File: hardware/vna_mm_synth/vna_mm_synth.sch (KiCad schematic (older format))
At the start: 0 parts

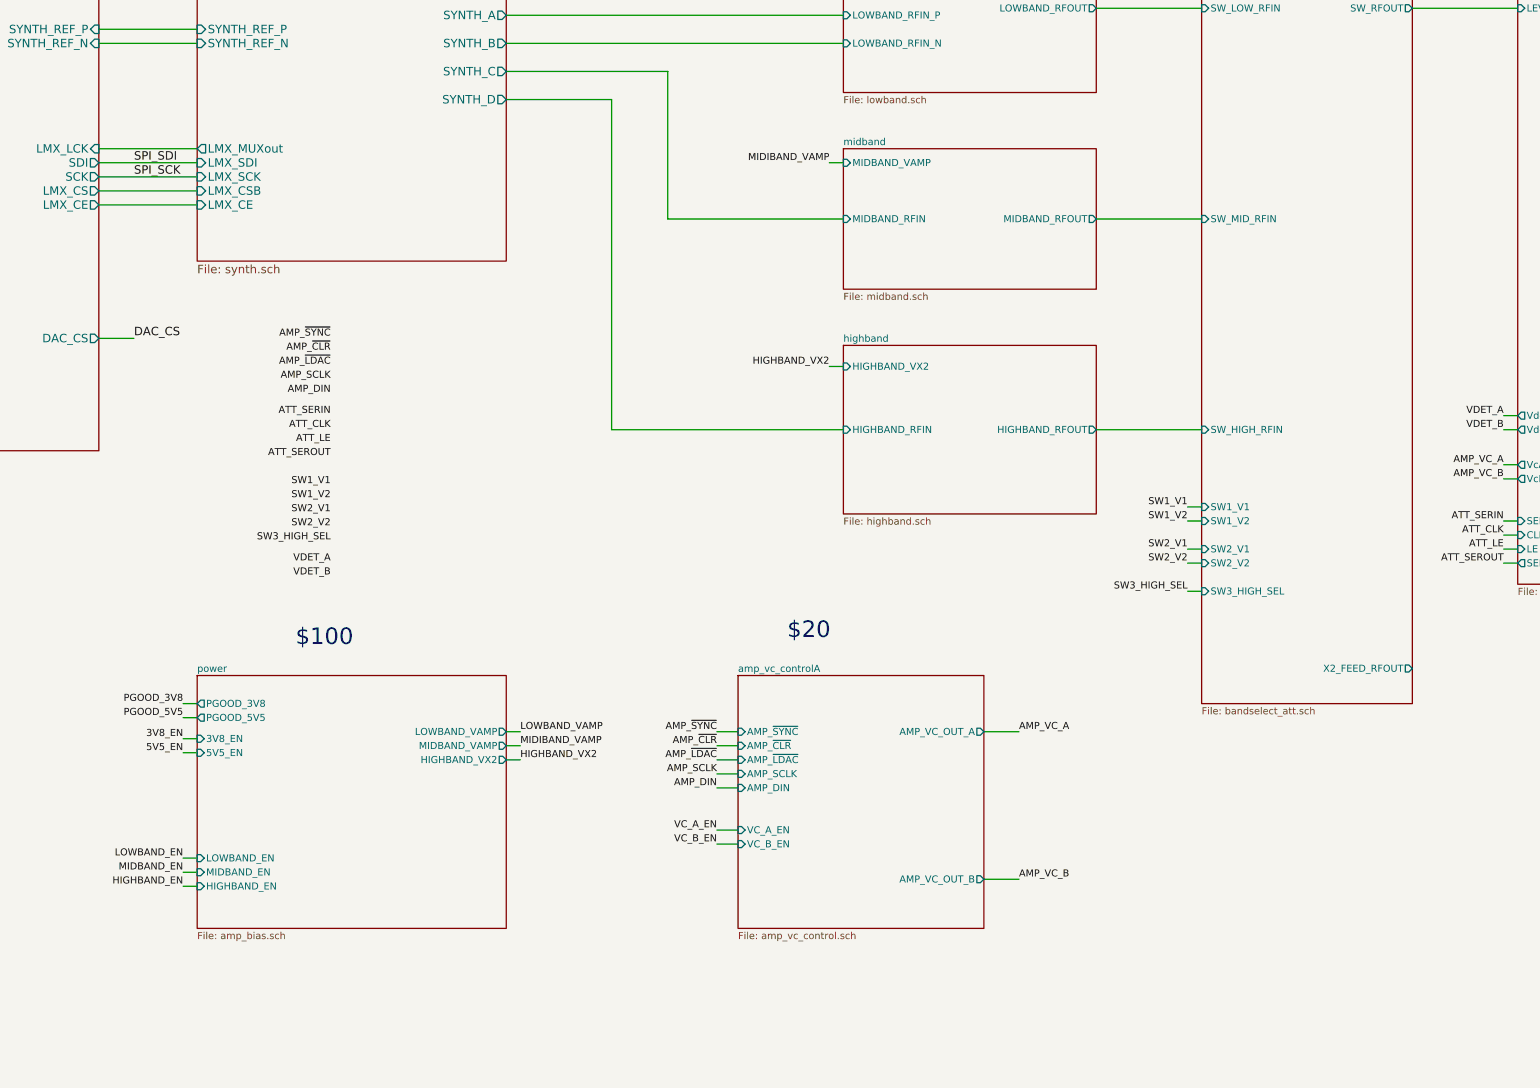
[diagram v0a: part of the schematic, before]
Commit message: changed synth midband filter bank to admv8416, added rf test points
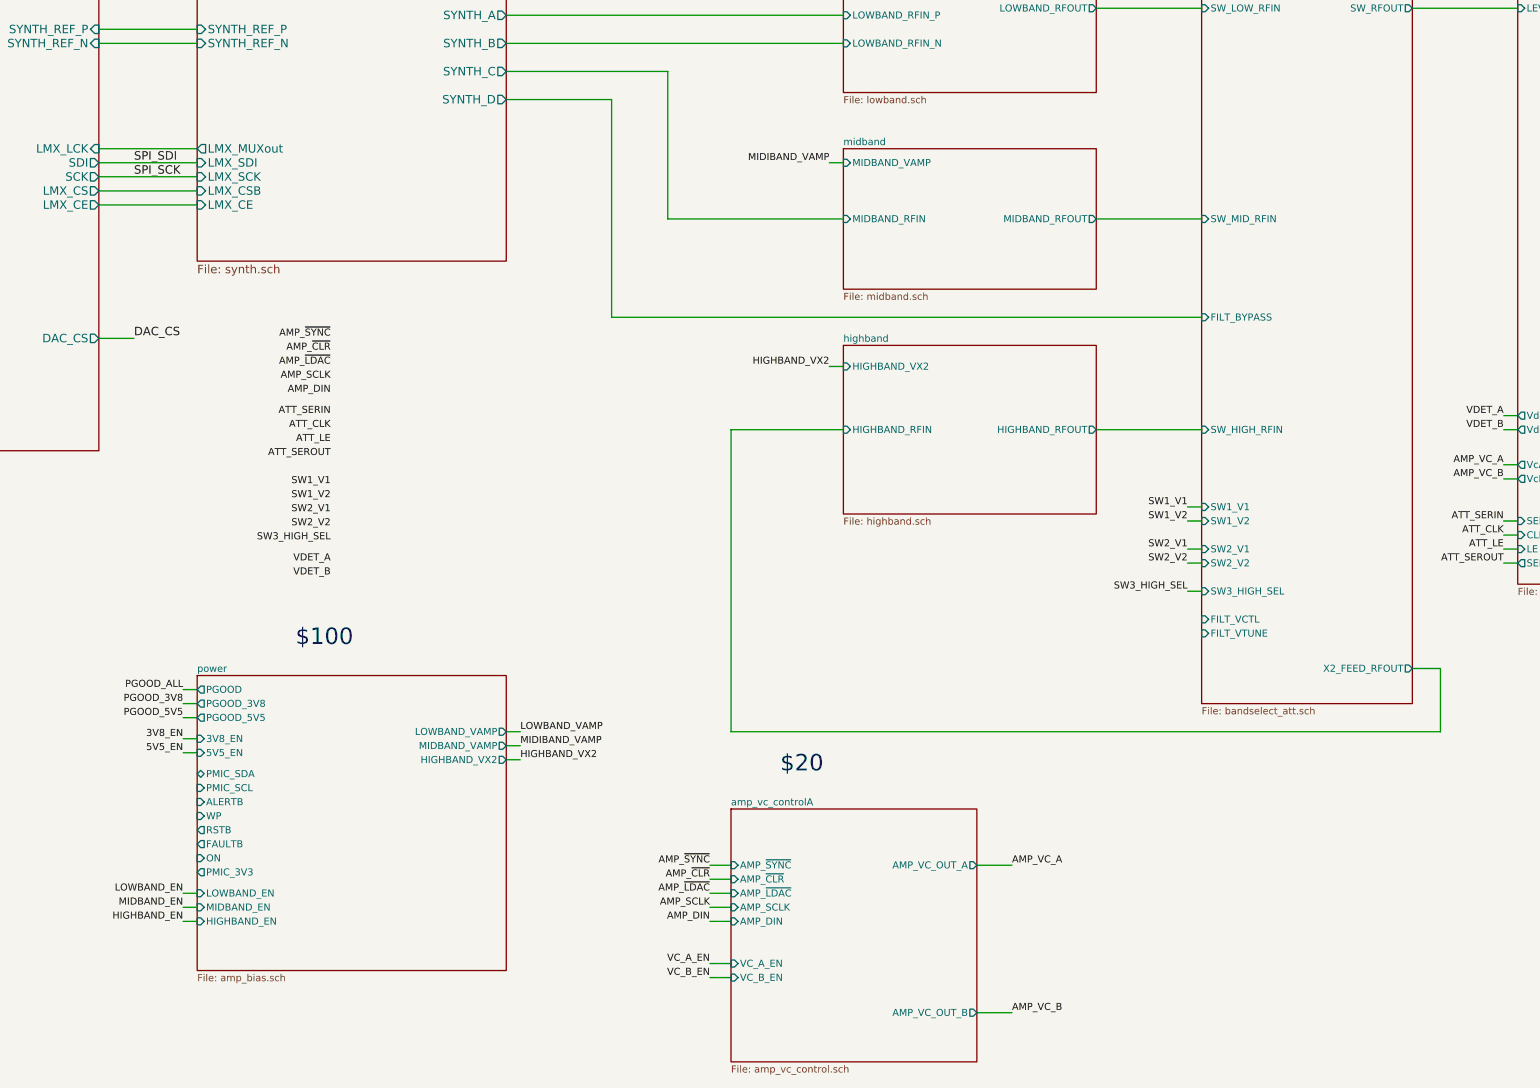
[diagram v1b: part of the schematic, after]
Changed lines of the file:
@@
 goals:\n400 MHz to 26.5 GHz (29 GHz)\n-15 dBc 2nd order harmonics\n-25 dBc 3rd order harmonics\n-15 to 0 dBm output power +/- 1 dB at room\nsettling time >1 ms to 90% amplitude\nphase sync with external reference\nBOM >$1000/each\nenclosure\nice40 fpga controlled?
 Wire Wire Line
-	11550 6050 9900 6050
-Wire Wire Line
-	9900 6050 9900 3700
+	11550 6050 10750 6050
 Wire Wire Line
 	9150 3700 9900 3700
@@
 Text Label 9250 8400 0    50   ~ 0
 HIGHBAND_VX2
-Text Label 12800 8200 0    50   ~ 0
+Text Label 12750 9150 0    50   ~ 0
 AMP_VC_A
-Text Label 12800 9250 0    50   ~ 0
+Text Label 12750 10200 0    50   ~ 0
 AMP_VC_B
 Text Label 11450 2750 2    50   ~ 0
@@
 F10 "SW1_V1" I L 14100 6600 50
 F11 "SW1_V2" I L 14100 6700 50
+F12 "FILT_VCTL" I L 14100 7400 50
+F13 "FILT_VTUNE" I L 14100 7500 50
+F14 "FILT_BYPASS" I L 14100 5250 50
 $EndSheet
 Text Label 14000 7000 2    50   ~ 0
@@
 SW3_HIGH_SEL
 $Sheet
-S 10800 7800 1750 1800
+S 10750 8750 1750 1800
 U 5D8E086E
 F0 "amp_vc_controlA" 50
 F1 "amp_vc_control.sch" 50
-F2 "AMP_VC_OUT_A" O R 12550 8200 50
-F3 "AMP_~SYNC" I L 10800 8200 50
-F4 "AMP_~CLR" I L 10800 8300 50
-F5 "AMP_~LDAC" I L 10800 8400 50
-F6 "AMP_SCLK" I L 10800 8500 50
-F7 "AMP_DIN" I L 10800 8600 50
-F8 "AMP_VC_OUT_B" O R 12550 9250 50
-F9 "VC_B_EN" I L 10800 9000 50
-F10 "VC_A_EN" I L 10800 8900 50
+F2 "AMP_VC_OUT_A" O R 12500 9150 50
+F3 "AMP_~SYNC" I L 10750 9150 50
+F4 "AMP_~CLR" I L 10750 9250 50
+F5 "AMP_~LDAC" I L 10750 9350 50
+F6 "AMP_SCLK" I L 10750 9450 50
+F7 "AMP_DIN" I L 10750 9550 50
+F8 "AMP_VC_OUT_B" O R 12500 10200 50
+F9 "VC_B_EN" I L 10750 9950 50
+F10 "VC_A_EN" I L 10750 9850 50
 $EndSheet
 Wire Wire Line
-	12550 8200 12800 8200
-Wire Wire Line
-	12550 9250 12800 9250
+	12500 9150 12750 9150
+Wire Wire Line
+	12500 10200 12750 10200
 $Sheet
-S 6950 7800 2200 1800
+S 6950 7800 2200 2100
 U 5D4AD94E
 F0 "power" 50
@@
 F7 "3V8_EN" I L 6950 8250 50
 F8 "5V5_EN" I L 6950 8350 50
-F9 "LOWBAND_EN" I L 6950 9100 50
-F10 "MIDBAND_EN" I L 6950 9200 50
-F11 "HIGHBAND_EN" I L 6950 9300 50
+F9 "LOWBAND_EN" I L 6950 9350 50
+F10 "MIDBAND_EN" I L 6950 9450 50
+F11 "HIGHBAND_EN" I L 6950 9550 50
+F12 "PGOOD" O L 6950 7900 50
+F13 "PMIC_SDA" B L 6950 8500 50
+F14 "PMIC_SCL" I L 6950 8600 50
+F15 "ALERTB" I L 6950 8700 50
+F16 "WP" I L 6950 8800 50
+F17 "RSTB" O L 6950 8900 50
+F18 "FAULTB" O L 6950 9000 50
+F19 "ON" I L 6950 9100 50
+F20 "PMIC_3V3" O L 6950 9200 50
 $EndSheet
 Wire Wire Line
-	10800 8200 10650 8200
-Wire Wire Line
-	10800 8300 10650 8300
-Text Label 10650 8200 2    50   ~ 0
+	10750 9150 10600 9150
+Wire Wire Line
+	10750 9250 10600 9250
+Text Label 10600 9150 2    50   ~ 0
 AMP_~SYNC
-Text Label 10650 8300 2    50   ~ 0
+Text Label 10600 9250 2    50   ~ 0
 AMP_~CLR
-Text Label 10650 8400 2    50   ~ 0
+Text Label 10600 9350 2    50   ~ 0
 AMP_~LDAC
-Text Label 10650 8500 2    50   ~ 0
+Text Label 10600 9450 2    50   ~ 0
 AMP_SCLK
-Text Label 10650 8600 2    50   ~ 0
+Text Label 10600 9550 2    50   ~ 0
 AMP_DIN
 Wire Wire Line
-	10650 8400 10800 8400
-Wire Wire Line
-	10650 8500 10800 8500
-Wire Wire Line
-	10650 8600 10800 8600
+	10600 9350 10750 9350
+Wire Wire Line
+	10600 9450 10750 9450
+Wire Wire Line
+	10600 9550 10750 9550
 Wire Wire Line
 	6950 8000 6850 8000
@@
 Wire Wire Line
 	6850 8350 6950 8350
-Text Label 6850 9100 2    50   ~ 0
+Text Label 6850 9350 2    50   ~ 0
 LOWBAND_EN
 Wire Wire Line
-	6850 9100 6950 9100
-Wire Wire Line
-	6850 9200 6950 9200
-Wire Wire Line
-	6850 9300 6950 9300
-Text Label 6850 9200 2    50   ~ 0
+	6850 9350 6950 9350
+Wire Wire Line
+	6850 9450 6950 9450
+Wire Wire Line
+	6850 9550 6950 9550
+Text Label 6850 9450 2    50   ~ 0
 MIDBAND_EN
-Text Label 6850 9300 2    50   ~ 0
+Text Label 6850 9550 2    50   ~ 0
 HIGHBAND_EN
 Text Label 7900 5400 2    50   ~ 0
@@
 Text Notes 7650 7600 0    118  ~ 0
 $100
-Text Notes 11150 7550 0    118  ~ 0
+Text Notes 11100 8500 0    118  ~ 0
 $20
 Text Label 7900 7000 2    50   ~ 0
@@
 Text Label 7900 7100 2    50   ~ 0
 VDET_B
-Text Label 10650 8900 2    50   ~ 0
+Text Label 10600 9850 2    50   ~ 0
 VC_A_EN
-Text Label 10650 9000 2    50   ~ 0
+Text Label 10600 9950 2    50   ~ 0
 VC_B_EN
 Wire Wire Line
-	10650 9000 10800 9000
-Wire Wire Line
-	10800 8900 10650 8900
+	10600 9950 10750 9950
+Wire Wire Line
+	10750 9850 10600 9850
+Text Label 6850 7900 2    50   ~ 0
+PGOOD_ALL
+Wire Wire Line
+	6850 7900 6950 7900
+Wire Wire Line
+	15600 7750 15800 7750
+Wire Wire Line
+	15800 7750 15800 8200
+Wire Wire Line
+	15800 8200 10750 8200
+Wire Wire Line
+	10750 8200 10750 6050
+Wire Wire Line
+	14100 5250 9900 5250
+Wire Wire Line
+	9900 5250 9900 3700
 $EndSCHEMATC

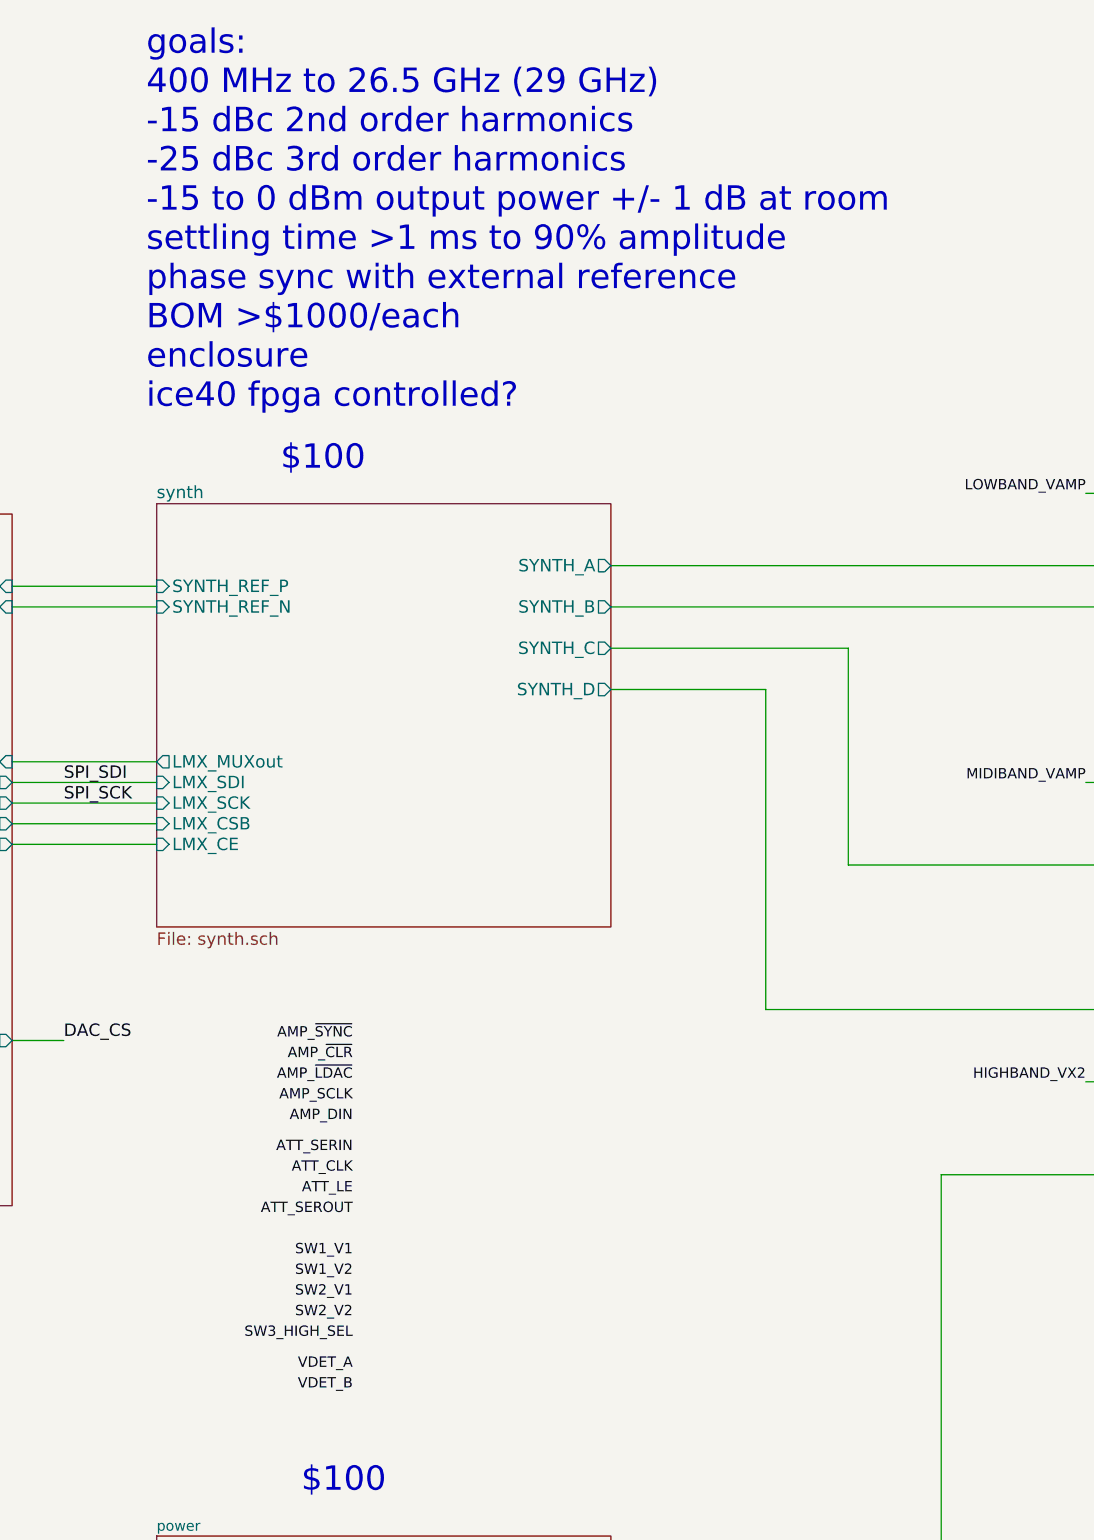
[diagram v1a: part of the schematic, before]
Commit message: added trl cal and set of breakout boards
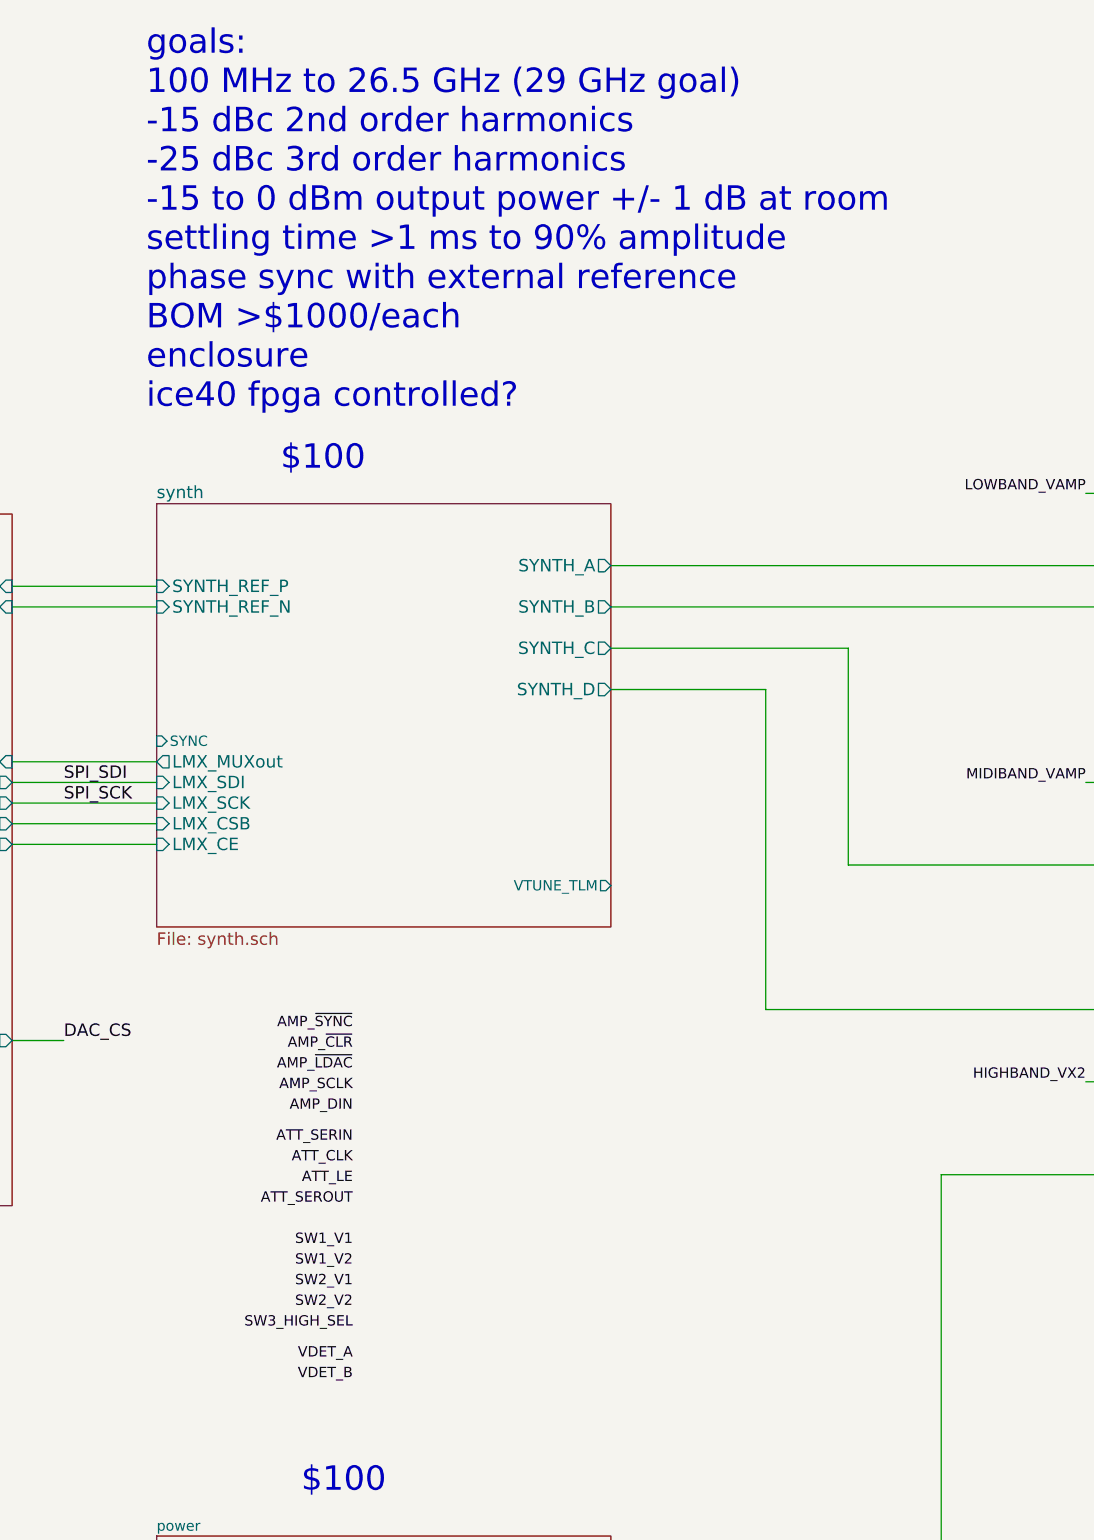
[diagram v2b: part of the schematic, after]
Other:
- note added: "goals:\n100 MHz to 26.5 GHz (29 GHz goal)\n-15 dBc 2nd order harmonics\n-25 dBc 3rd order harmonics\n-15 to 0 dBm output power +/- 1 dB at room\nsettling time >1 ms to 90% amplitude\nphase sync with external reference\nBOM >$1000/each\nenclosure\nice40 fpga controlled?"
- note removed: "goals:\n400 MHz to 26.5 GHz (29 GHz)\n-15 dBc 2nd order harmonics\n-25 dBc 3rd order harmonics\n-15 to 0 dBm output power +/- 1 dB at room\nsettling time >1 ms to 90% amplitude\nphase sync with external reference\nBOM >$1000/each\nenclosure\nice40 fpga controlled?"
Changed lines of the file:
@@
 F11 "LMX_SDI" I L 6950 4150 60
 F12 "LMX_SCK" I L 6950 4250 60
+F13 "SYNC" I L 6950 3950 50
+F14 "VTUNE_TLM" O R 9150 4650 50
 $EndSheet
 $Sheet
@@
 $EndSheet
 Text Notes 6900 2350 0    118  ~ 0
-goals:\n400 MHz to 26.5 GHz (29 GHz)\n-15 dBc 2nd order harmonics\n-25 dBc 3rd order harmonics\n-15 to 0 dBm output power +/- 1 dB at room\nsettling time >1 ms to 90% amplitude\nphase sync with external reference\nBOM >$1000/each\nenclosure\nice40 fpga controlled?
+goals:\n100 MHz to 26.5 GHz (29 GHz goal)\n-15 dBc 2nd order harmonics\n-25 dBc 3rd order harmonics\n-15 to 0 dBm output power +/- 1 dB at room\nsettling time >1 ms to 90% amplitude\nphase sync with external reference\nBOM >$1000/each\nenclosure\nice40 fpga controlled?
 Wire Wire Line
 	11550 6050 10750 6050
@@
 Wire Wire Line
 	16250 7000 16350 7000
-Text Label 7900 5950 2    50   ~ 0
+Text Label 7900 5900 2    50   ~ 0
 ATT_SERIN
-Text Label 7900 6050 2    50   ~ 0
+Text Label 7900 6000 2    50   ~ 0
 ATT_CLK
-Text Label 7900 6150 2    50   ~ 0
+Text Label 7900 6100 2    50   ~ 0
 ATT_LE
-Text Label 7900 6250 2    50   ~ 0
+Text Label 7900 6200 2    50   ~ 0
 ATT_SEROUT
 Wire Wire Line
@@
 Text Label 14000 7200 2    50   ~ 0
 SW3_HIGH_SEL
-Text Label 7900 6450 2    50   ~ 0
+Text Label 7900 6400 2    50   ~ 0
 SW1_V1
-Text Label 7900 6550 2    50   ~ 0
+Text Label 7900 6500 2    50   ~ 0
 SW1_V2
-Text Label 7900 6650 2    50   ~ 0
+Text Label 7900 6600 2    50   ~ 0
 SW2_V1
-Text Label 7900 6750 2    50   ~ 0
+Text Label 7900 6700 2    50   ~ 0
 SW2_V2
-Text Label 7900 6850 2    50   ~ 0
+Text Label 7900 6800 2    50   ~ 0
 SW3_HIGH_SEL
 $Sheet
@@
 Text Label 6850 9550 2    50   ~ 0
 HIGHBAND_EN
-Text Label 7900 5400 2    50   ~ 0
+Text Label 7900 5350 2    50   ~ 0
 AMP_~SYNC
-Text Label 7900 5500 2    50   ~ 0
+Text Label 7900 5450 2    50   ~ 0
 AMP_~CLR
-Text Label 7900 5600 2    50   ~ 0
+Text Label 7900 5550 2    50   ~ 0
 AMP_~LDAC
-Text Label 7900 5700 2    50   ~ 0
+Text Label 7900 5650 2    50   ~ 0
 AMP_SCLK
-Text Label 7900 5800 2    50   ~ 0
+Text Label 7900 5750 2    50   ~ 0
 AMP_DIN
 Text Notes 7650 7600 0    118  ~ 0
@@
 Text Notes 11100 8500 0    118  ~ 0
 $20
-Text Label 7900 7000 2    50   ~ 0
+Text Label 7900 6950 2    50   ~ 0
 VDET_A
-Text Label 7900 7100 2    50   ~ 0
+Text Label 7900 7050 2    50   ~ 0
 VDET_B
 Text Label 10600 9850 2    50   ~ 0
